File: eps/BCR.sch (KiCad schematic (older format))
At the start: 12 parts, among them J1 SA1A, J2 SA1B, J3 SA2A, J4 SA2B, J5 SA3A, J6 SA3B

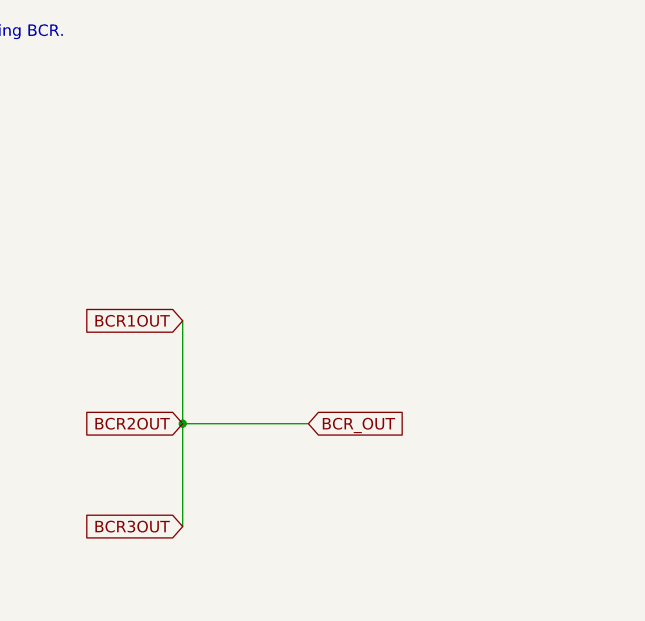
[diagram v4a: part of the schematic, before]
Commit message: implement PDM LCLs
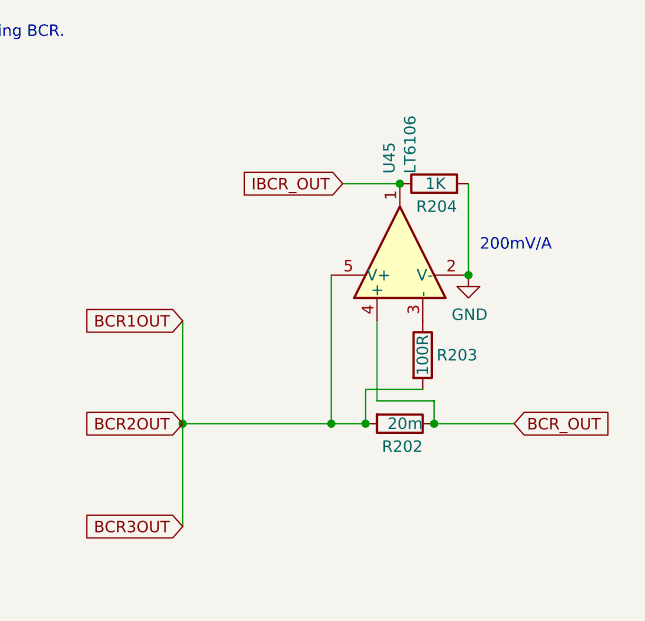
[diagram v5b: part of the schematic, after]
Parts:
- added R202: 20m, symbol Device:R
- added R203: 100R, symbol Device:R
- added R204: 1K, symbol Device:R
- added U45: LT6106, Package_TO_SOT_SMD:SOT-23-5, symbol Amplifier_Current:LT6106
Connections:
- net BCR1OUT: now also R202.2, R203.2, U45.5 (V+)
- net GND: now also R204.2, U45.2 (V-)
- new net: R203.1, U45.3 (-)
- new net BCR_OUT: R202.1, U45.4 (+)
- new net IBCR_OUT: R204.1, U45.1
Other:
- note added: "200mV/A\n"
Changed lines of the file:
@@
 Wire Wire Line
 	5450 2550 5450 3000
-Wire Wire Line
-	5450 3000 6000 3000
 Connection ~ 5450 3000
 Wire Wire Line
 	5450 3000 5450 3450
-Text GLabel 6000 3000 2    50   Input ~ 0
+Text GLabel 6900 3000 2    50   Input ~ 0
 BCR_OUT
+$Comp
+L Device:R R?
+U 1 1 61877BC1
+P 6400 3000
+AR Path="/61928B56/61877BC1" Ref="R?"  Part="1"
+AR Path="/61929CC0/6194502F/61877BC1" Ref="R?"  Part="1"
+AR Path="/61929CC0/61964B2B/61877BC1" Ref="R?"  Part="1"
+AR Path="/61929CC0/61964D92/61877BC1" Ref="R?"  Part="1"
+AR Path="/61929CC0/61877BC1" Ref="R202"  Part="1"
+F 0 "R202" V 6500 3100 50  0000 R CNN
+F 1 "20m" V 6400 3100 50  0000 R CNN
+F 2 "" V 6330 3000 50  0001 C CNN
+F 3 "~" H 6400 3000 50  0001 C CNN
+	1    6400 3000
+	0    1    1    0
+$EndComp
+$Comp
+L Amplifier_Current:LT6106 U?
+U 1 1 61877BC7
+P 6400 2250
+AR Path="/61928B56/61877BC7" Ref="U?"  Part="1"
+AR Path="/61929CC0/6194502F/61877BC7" Ref="U?"  Part="1"
+AR Path="/61929CC0/61964B2B/61877BC7" Ref="U?"  Part="1"
+AR Path="/61929CC0/61964D92/61877BC7" Ref="U?"  Part="1"
+AR Path="/61929CC0/61877BC7" Ref="U45"  Part="1"
+F 0 "U45" H 6744 2296 50  0000 L CNN
+F 1 "LT6106" H 6744 2205 50  0000 L CNN
+F 2 "Package_TO_SOT_SMD:SOT-23-5" H 6400 2250 50  0001 C CNN
+F 3 "https://www.analog.com/media/en/technical-documentation/data-sheets/6106fb.pdf" H 6450 2450 50  0001 C CNN
+	1    6400 2250
+	0    -1   -1   0
+$EndComp
+$Comp
+L power:GND #PWR?
+U 1 1 61877BCD
+P 6700 2350
+AR Path="/61928B56/61877BCD" Ref="#PWR?"  Part="1"
+AR Path="/61929CC0/6194502F/61877BCD" Ref="#PWR?"  Part="1"
+AR Path="/61929CC0/61964B2B/61877BCD" Ref="#PWR?"  Part="1"
+AR Path="/61929CC0/61964D92/61877BCD" Ref="#PWR?"  Part="1"
+AR Path="/61929CC0/61877BCD" Ref="#PWR0185"  Part="1"
+F 0 "#PWR0185" H 6700 2100 50  0001 C CNN
+F 1 "GND" H 6705 2177 50  0000 C CNN
+F 2 "" H 6700 2350 50  0001 C CNN
+F 3 "" H 6700 2350 50  0001 C CNN
+	1    6700 2350
+	1    0    0    -1
+$EndComp
+$Comp
+L Device:R R?
+U 1 1 61877BD3
+P 6550 1950
+AR Path="/61928B56/61877BD3" Ref="R?"  Part="1"
+AR Path="/61929CC0/6194502F/61877BD3" Ref="R?"  Part="1"
+AR Path="/61929CC0/61964B2B/61877BD3" Ref="R?"  Part="1"
+AR Path="/61929CC0/61964D92/61877BD3" Ref="R?"  Part="1"
+AR Path="/61929CC0/61877BD3" Ref="R204"  Part="1"
+F 0 "R204" V 6450 1850 50  0000 L CNN
+F 1 "1K" V 6550 1900 50  0000 L CNN
+F 2 "" V 6480 1950 50  0001 C CNN
+F 3 "~" H 6550 1950 50  0001 C CNN
+	1    6550 1950
+	0    -1   -1   0
+$EndComp
+Wire Wire Line
+	6700 1950 6700 2350
+Connection ~ 6700 2350
+Wire Wire Line
+	6100 3000 6100 2350
+$Comp
+L Device:R R?
+U 1 1 61877BDC
+P 6500 2700
+AR Path="/61928B56/61877BDC" Ref="R?"  Part="1"
+AR Path="/61929CC0/6194502F/61877BDC" Ref="R?"  Part="1"
+AR Path="/61929CC0/61964B2B/61877BDC" Ref="R?"  Part="1"
+AR Path="/61929CC0/61964D92/61877BDC" Ref="R?"  Part="1"
+AR Path="/61929CC0/61877BDC" Ref="R203"  Part="1"
+F 0 "R203" H 6650 2700 50  0000 C CNN
+F 1 "100R" V 6500 2700 50  0000 C CNN
+F 2 "" V 6430 2700 50  0001 C CNN
+F 3 "~" H 6500 2700 50  0001 C CNN
+	1    6500 2700
+	1    0    0    -1
+$EndComp
+Wire Wire Line
+	6300 2550 6300 2900
+Wire Wire Line
+	6300 2900 6550 2900
+Wire Wire Line
+	6550 2900 6550 3000
+Wire Wire Line
+	6500 2850 6250 2850
+Wire Wire Line
+	6250 2850 6250 3000
+Wire Wire Line
+	6250 3000 6100 3000
+Connection ~ 6250 3000
+Text Notes 6750 2250 0    50   ~ 0
+200mV/A\n
+Wire Wire Line
+	6550 3000 6900 3000
+Connection ~ 6100 3000
+Connection ~ 6550 3000
+Wire Wire Line
+	6400 1950 6150 1950
+Connection ~ 6400 1950
+Text GLabel 6150 1950 0    50   Input ~ 0
+IBCR_OUT
+Wire Wire Line
+	5450 3000 6100 3000
 $EndSCHEMATC

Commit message: update pcbnew
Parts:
- R125, R126, R127, R128, R129, R130, R202, R203, R204: footprint (none) -> Resistor_SMD:R_0805_2012Metric_Pad1.20x1.40mm_HandSolder
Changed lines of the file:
@@
 F 0 "R125" H 2000 1600 50  0000 L CNN
 F 1 "100K" V 1950 1500 50  0000 L CNN
-F 2 "" V 1880 1600 50  0001 C CNN
+F 2 "Resistor_SMD:R_0805_2012Metric_Pad1.20x1.40mm_HandSolder" V 1880 1600 50  0001 C CNN
 F 3 "~" H 1950 1600 50  0001 C CNN
 	1    1950 1600
@@
 F 0 "R126" H 2000 2350 50  0000 L CNN
 F 1 "100K" V 1950 2250 50  0000 L CNN
-F 2 "" V 1880 2350 50  0001 C CNN
+F 2 "Resistor_SMD:R_0805_2012Metric_Pad1.20x1.40mm_HandSolder" V 1880 2350 50  0001 C CNN
 F 3 "~" H 1950 2350 50  0001 C CNN
 	1    1950 2350
@@
 F 0 "R127" H 2000 3100 50  0000 L CNN
 F 1 "100K" V 1950 3000 50  0000 L CNN
-F 2 "" V 1880 3100 50  0001 C CNN
+F 2 "Resistor_SMD:R_0805_2012Metric_Pad1.20x1.40mm_HandSolder" V 1880 3100 50  0001 C CNN
 F 3 "~" H 1950 3100 50  0001 C CNN
 	1    1950 3100
@@
 F 0 "R128" H 2000 3850 50  0000 L CNN
 F 1 "100K" V 1950 3750 50  0000 L CNN
-F 2 "" V 1880 3850 50  0001 C CNN
+F 2 "Resistor_SMD:R_0805_2012Metric_Pad1.20x1.40mm_HandSolder" V 1880 3850 50  0001 C CNN
 F 3 "~" H 1950 3850 50  0001 C CNN
 	1    1950 3850
@@
 F 0 "R129" H 2000 4600 50  0000 L CNN
 F 1 "100K" V 1950 4500 50  0000 L CNN
-F 2 "" V 1880 4600 50  0001 C CNN
+F 2 "Resistor_SMD:R_0805_2012Metric_Pad1.20x1.40mm_HandSolder" V 1880 4600 50  0001 C CNN
 F 3 "~" H 1950 4600 50  0001 C CNN
 	1    1950 4600
@@
 F 0 "R130" H 2000 5350 50  0000 L CNN
 F 1 "100K" V 1950 5250 50  0000 L CNN
-F 2 "" V 1880 5350 50  0001 C CNN
+F 2 "Resistor_SMD:R_0805_2012Metric_Pad1.20x1.40mm_HandSolder" V 1880 5350 50  0001 C CNN
 F 3 "~" H 1950 5350 50  0001 C CNN
 	1    1950 5350
@@
 F 0 "R202" V 6500 3100 50  0000 R CNN
 F 1 "20m" V 6400 3100 50  0000 R CNN
-F 2 "" V 6330 3000 50  0001 C CNN
+F 2 "Resistor_SMD:R_0805_2012Metric_Pad1.20x1.40mm_HandSolder" V 6330 3000 50  0001 C CNN
 F 3 "~" H 6400 3000 50  0001 C CNN
 	1    6400 3000
@@
 F 0 "R204" V 6450 1850 50  0000 L CNN
 F 1 "1K" V 6550 1900 50  0000 L CNN
-F 2 "" V 6480 1950 50  0001 C CNN
+F 2 "Resistor_SMD:R_0805_2012Metric_Pad1.20x1.40mm_HandSolder" V 6480 1950 50  0001 C CNN
 F 3 "~" H 6550 1950 50  0001 C CNN
 	1    6550 1950
@@
 F 0 "R203" H 6650 2700 50  0000 C CNN
 F 1 "100R" V 6500 2700 50  0000 C CNN
-F 2 "" V 6430 2700 50  0001 C CNN
+F 2 "Resistor_SMD:R_0805_2012Metric_Pad1.20x1.40mm_HandSolder" V 6430 2700 50  0001 C CNN
 F 3 "~" H 6500 2700 50  0001 C CNN
 	1    6500 2700
